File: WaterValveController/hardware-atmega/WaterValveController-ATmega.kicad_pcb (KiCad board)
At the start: 2 copper layers, 57 x 56 mm, 80 parts, among them J1 12V DC IN, J10 ICSP, J2 MAIN SWITCH, J3 VALVE / FLOW, J4 ESP32, J5 BUTTON, J6 LED 25L, J7 LED 50L, J8 LED 100L, J9 USB-C, Q1 AO4407A, Q2 2N7002, Q3 AO4407A, U1 TPS54202H, U2 RX480E-4, U3 CH340N, U4 ATmega328P-AU, Y1 16MHz

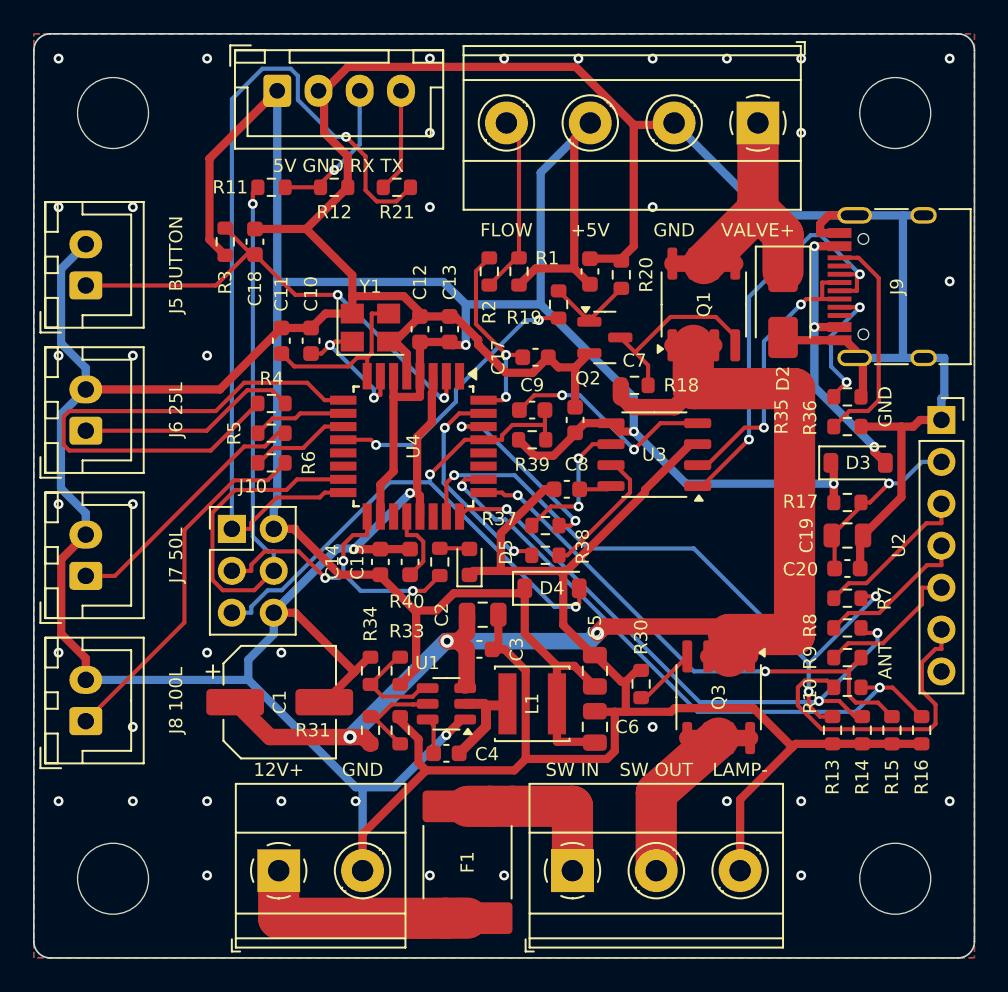
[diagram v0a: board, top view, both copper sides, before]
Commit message: ATmega board: room for a 6-pin ISP cable, programmer instructions
- J10 (ICSP) moves 2.5 mm up, with the LED resistors and the button
  pull-up/filter rearranged, so a 6-pin ribbon-cable plug clears C1; J10
  gets an ICSP label. Rerouted: 0 DRC errors, 0 unconnected.
- README: J10 pinout, what is on the ISP lines, and step-by-step bootloader
  burning with a Pololu USB AVR Programmer v2.1 (recommended) or a Nano as
  ISP (with the 10 uF reset capacitor), plus notes on USBasp clones.

Co-Authored-By: Claude Opus 5.5 <noreply@anthropic.com>
Claude-Session: https://claude.ai/code/session_01AqRGusXgpSip5brBmMU9hY
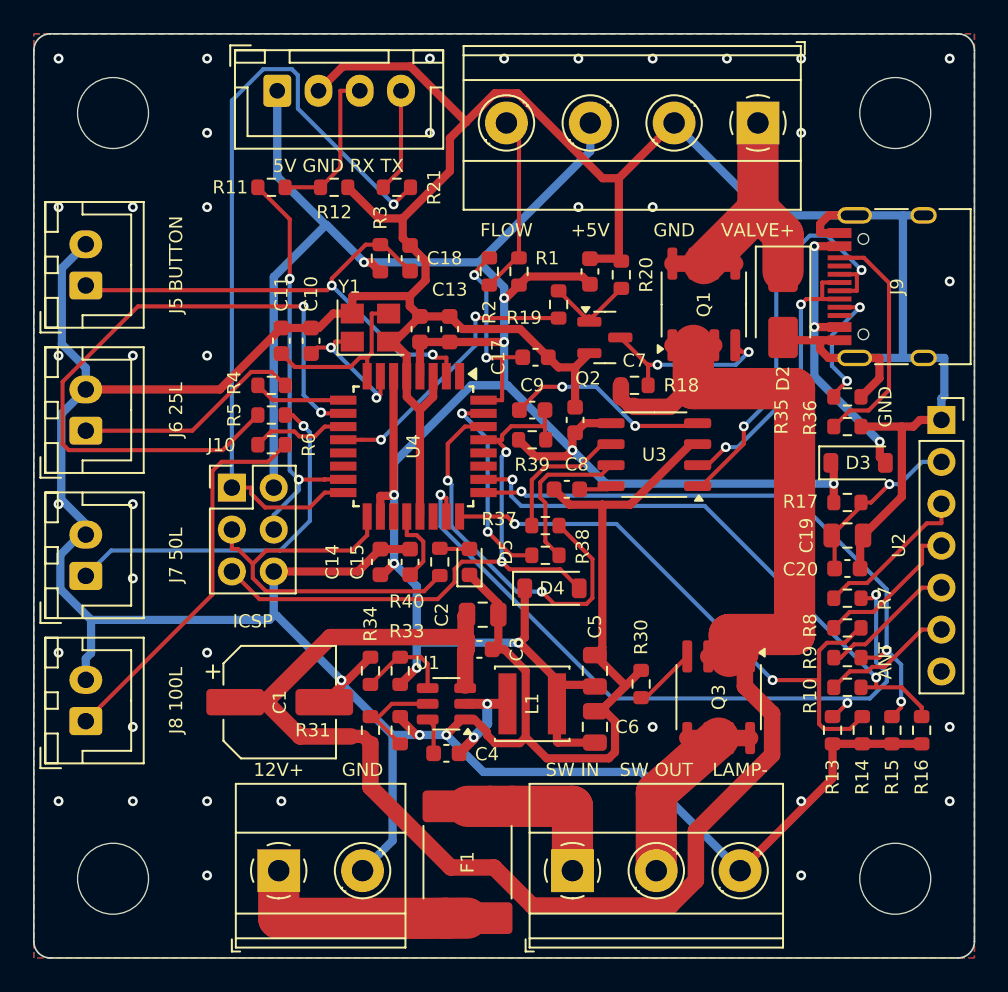
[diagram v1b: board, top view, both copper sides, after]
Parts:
- moved R3 9.45 mm to (121.0, 73.6)
- moved C18 9.45 mm to (122.8, 73.6)
- moved J10 2.50 mm to (112.0, 87.5)
- moved R4 1.10 mm to (114.4, 81.3)
- moved R5 1.10 mm to (114.4, 83.1)
- moved R6 1.10 mm to (114.4, 84.9)
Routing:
- net /LED50: track 5.67 -> 41.4 mm, vias 0 -> 2
- net +12V: track 80.7 -> 109.6 mm, vias 3 -> 0
- net /LED25: track 33.0 -> 5.55 mm
- net GND: track 361.6 -> 342.8 mm, vias 41 -> 40
- net /TX_5V: track 41.4 -> 25.1 mm, vias 1 -> 2
- net +5V: track 173.2 -> 157.5 mm, vias 3 -> 9
- net /RXD: track 11.7 -> 23.6 mm
- net /RX_D3: track 19.4 -> 7.97 mm
- net /LED50_A: track 15.7 -> 22.3 mm, vias 0 -> 1
- net /SCK: track 19.5 -> 24.5 mm, vias 3 -> 0
- net /RF3: track 32.4 -> 37.0 mm, vias 2 -> 3
- net /RF1: track 39.9 -> 43.3 mm
- net /ESP_IN: track 51.2 -> 47.9 mm
- net /RF4: track 37.6 -> 34.8 mm
- net /BTN: track 29.6 -> 31.7 mm
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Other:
- board text added: "ICSP"
